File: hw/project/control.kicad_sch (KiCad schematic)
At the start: 44 parts, among them SW1 BOOT0, SW2 RESET, U1 STSPIN32G4, X1 SWXC5ACVF0-32.000000

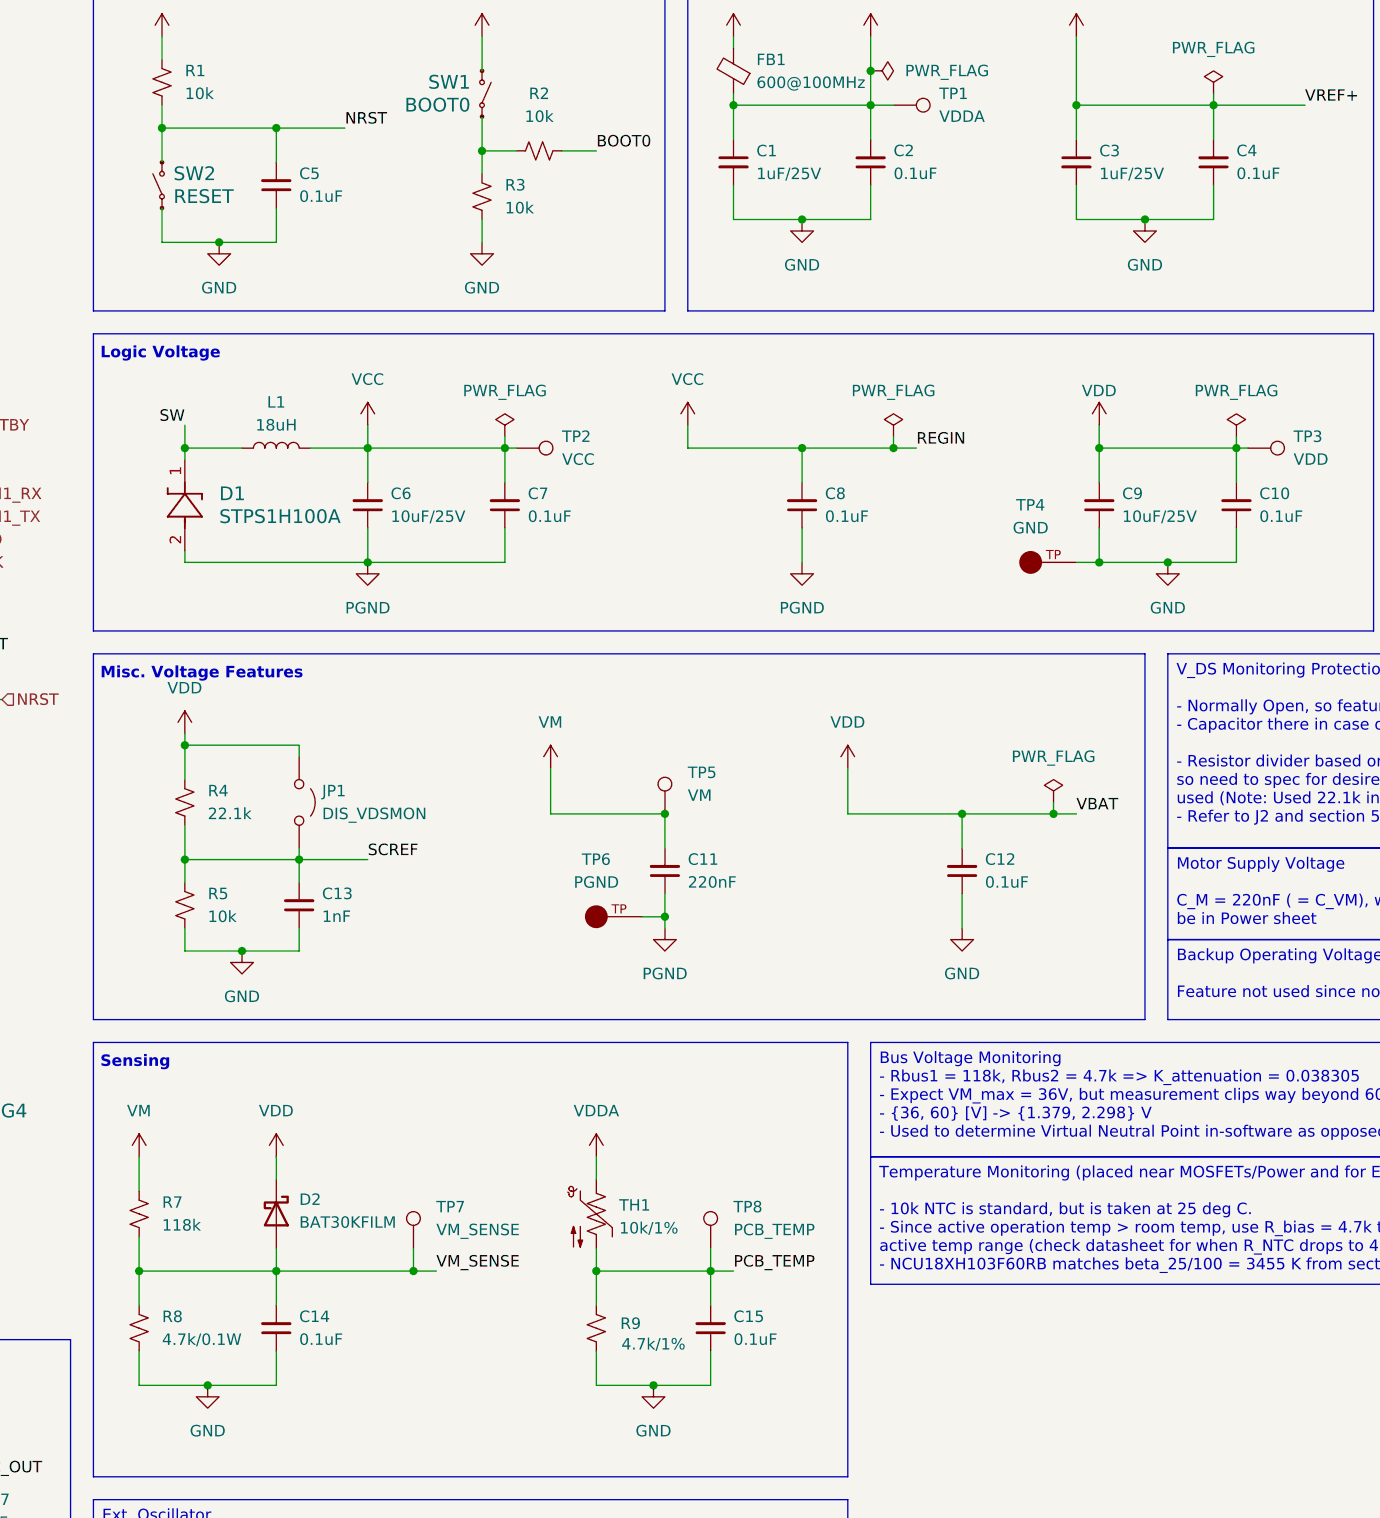
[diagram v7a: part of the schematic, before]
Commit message: Update all components to LCSC version/alternative!
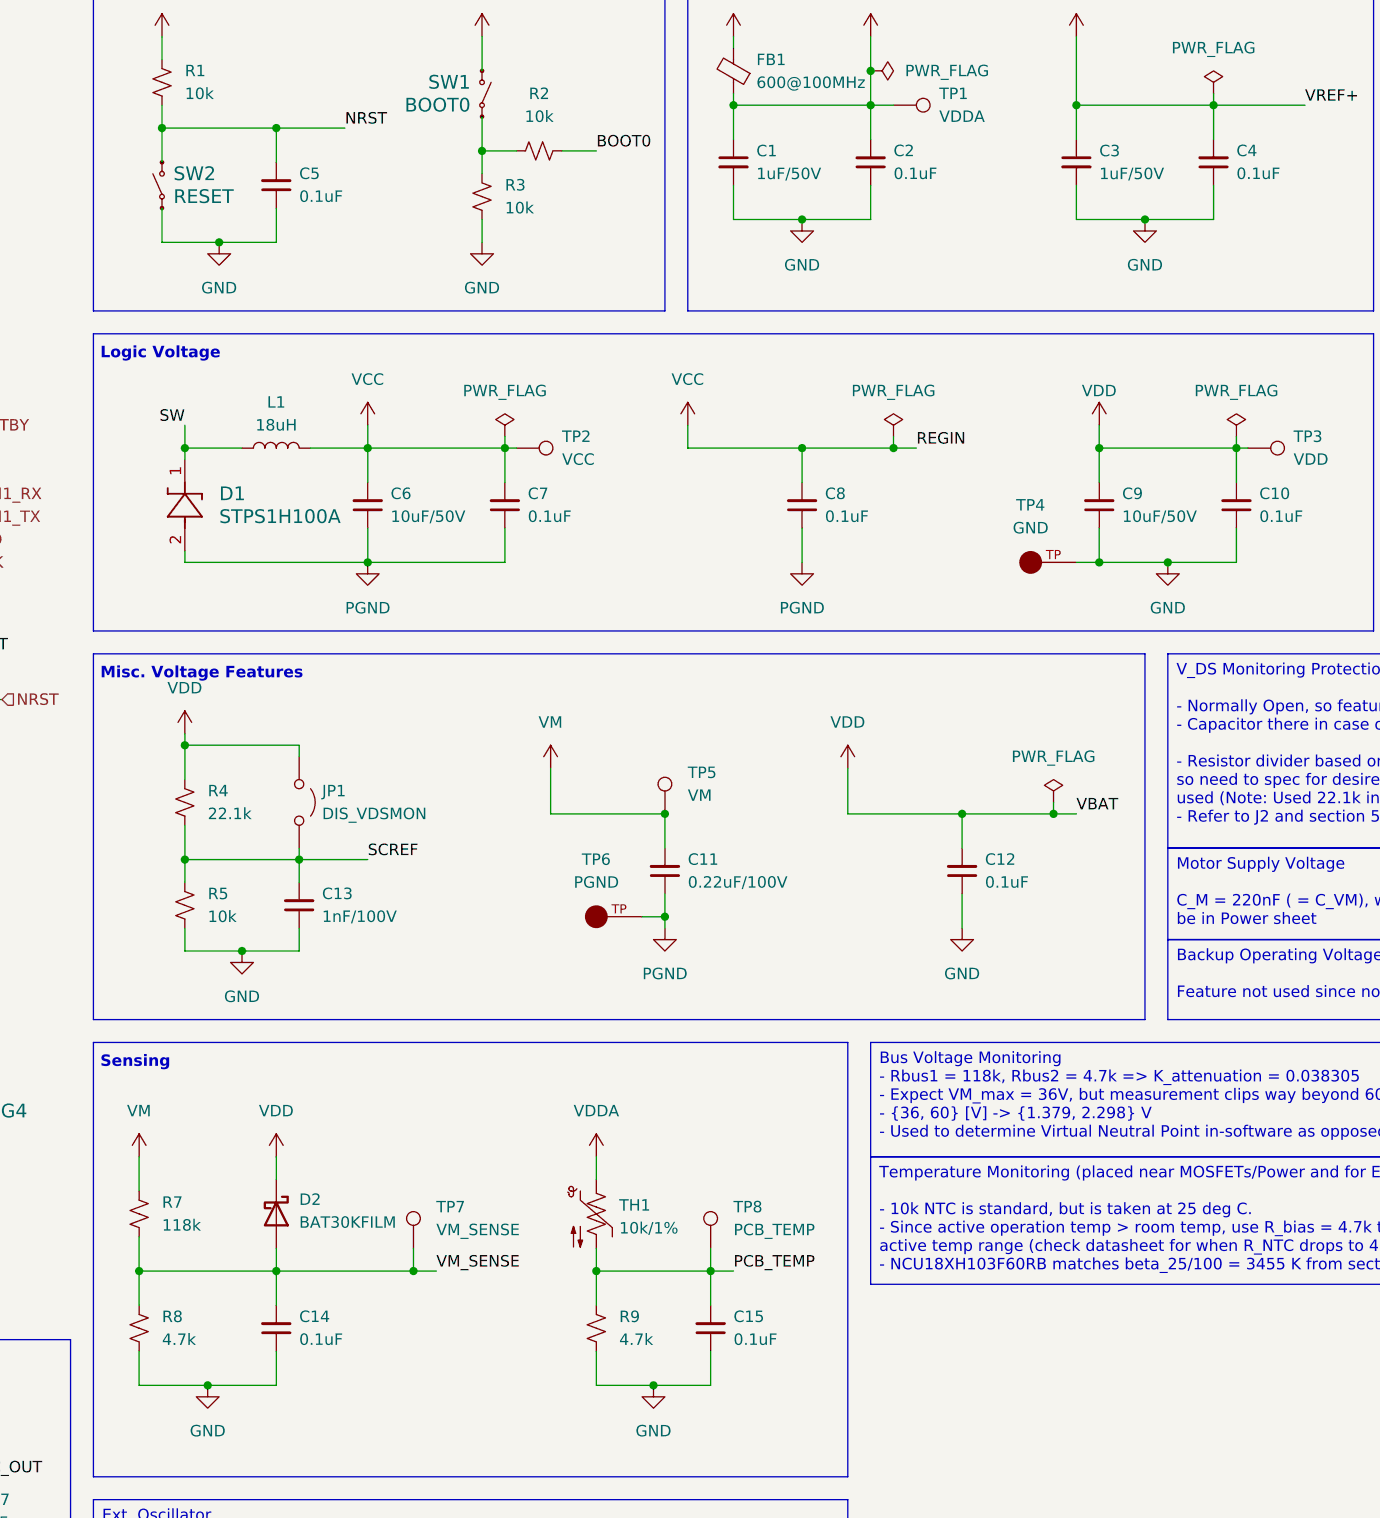
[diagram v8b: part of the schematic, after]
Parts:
- C1, C3: value 1uF/25V -> 1uF/50V; JLCPCB (none) -> https://jlcpcb.com/partdetail/16531-CL10A105KB8NNNC/C15849; LCSC (none) -> C15849
- C10, C12, C14, C15, C2, C4, C5, C7, C8: JLCPCB (none) -> https://jlcpcb.com/partdetail/16407-CL10B104KC8NNNC/C15725; LCSC (none) -> C15725
- C11: value 220nF -> 0.22uF/100V; JLCPCB (none) -> https://jlcpcb.com/partdetail/TaiyoYuden-HMK107C7224KAHTE/C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; LCSC (none) -> C2169715
- C13: value 1nF -> 1nF/100V; JLCPCB (none) -> https://jlcpcb.com/partdetail/YAGEO-CC0603JRNPO0BN102/C1137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; LCSC (none) -> C113793
- C6, C9: value 10uF/25V -> 10uF/50V; JLCPCB (none) -> https://jlcpcb.com/partdetail/439567-GRM21BR61H106KE43L/C44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; LCSC (none) -> C440198
- JP1: JLCPCB (none) -> https://jlcpcb.com/partdetail/AmphenolICC-G800W306018EU/C54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; LCSC (none) -> C5426960
- R1, R2, R3, R5: JLCPCB (none) -> https://jlcpcb.com/partdetail/26547-0603WAF1002T5E/C25804; LCSC (none) -> C25804
- R4: JLCPCB (none) -> https://jlcpcb.com/partdetail/26704-0603WAF2212T5E/C25961; LCSC (none) -> C25961
- R6: JLCPCB (none) -> https://jlcpcb.com/partdetail/21903-0603WAF0000T5E/C21189; LCSC (none) -> C21189
- R7: JLCPCB (none) -> https://jlcpcb.com/partdetail/26549-0603WAF1183T5E/C25806; LCSC (none) -> C25806
- R8: value 4.7k/0.1W -> 4.7k; JLCPCB (none) -> https://jlcpcb.com/partdetail/23889-0603WAF4701T5E/C23162; LCSC (none) -> C23162
- R9: value 4.7k/1% -> 4.7k; JLCPCB (none) -> https://jlcpcb.com/partdetail/23889-0603WAF4701T5E/C23162; LCSC (none) -> C23162
